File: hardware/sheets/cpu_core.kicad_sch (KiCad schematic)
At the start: 32 parts, among them U1 V20, U10 74HCT32, U11 74HCT125, U12 74HC157, U13 74HCT04, U14 TCM809, U2 74HCT573, U3 74HCT573, U4 74HCT573, U5 74HCT245, U6 74HCT138, U7 74HCT00, U8 74HCT74, U9 74HC161

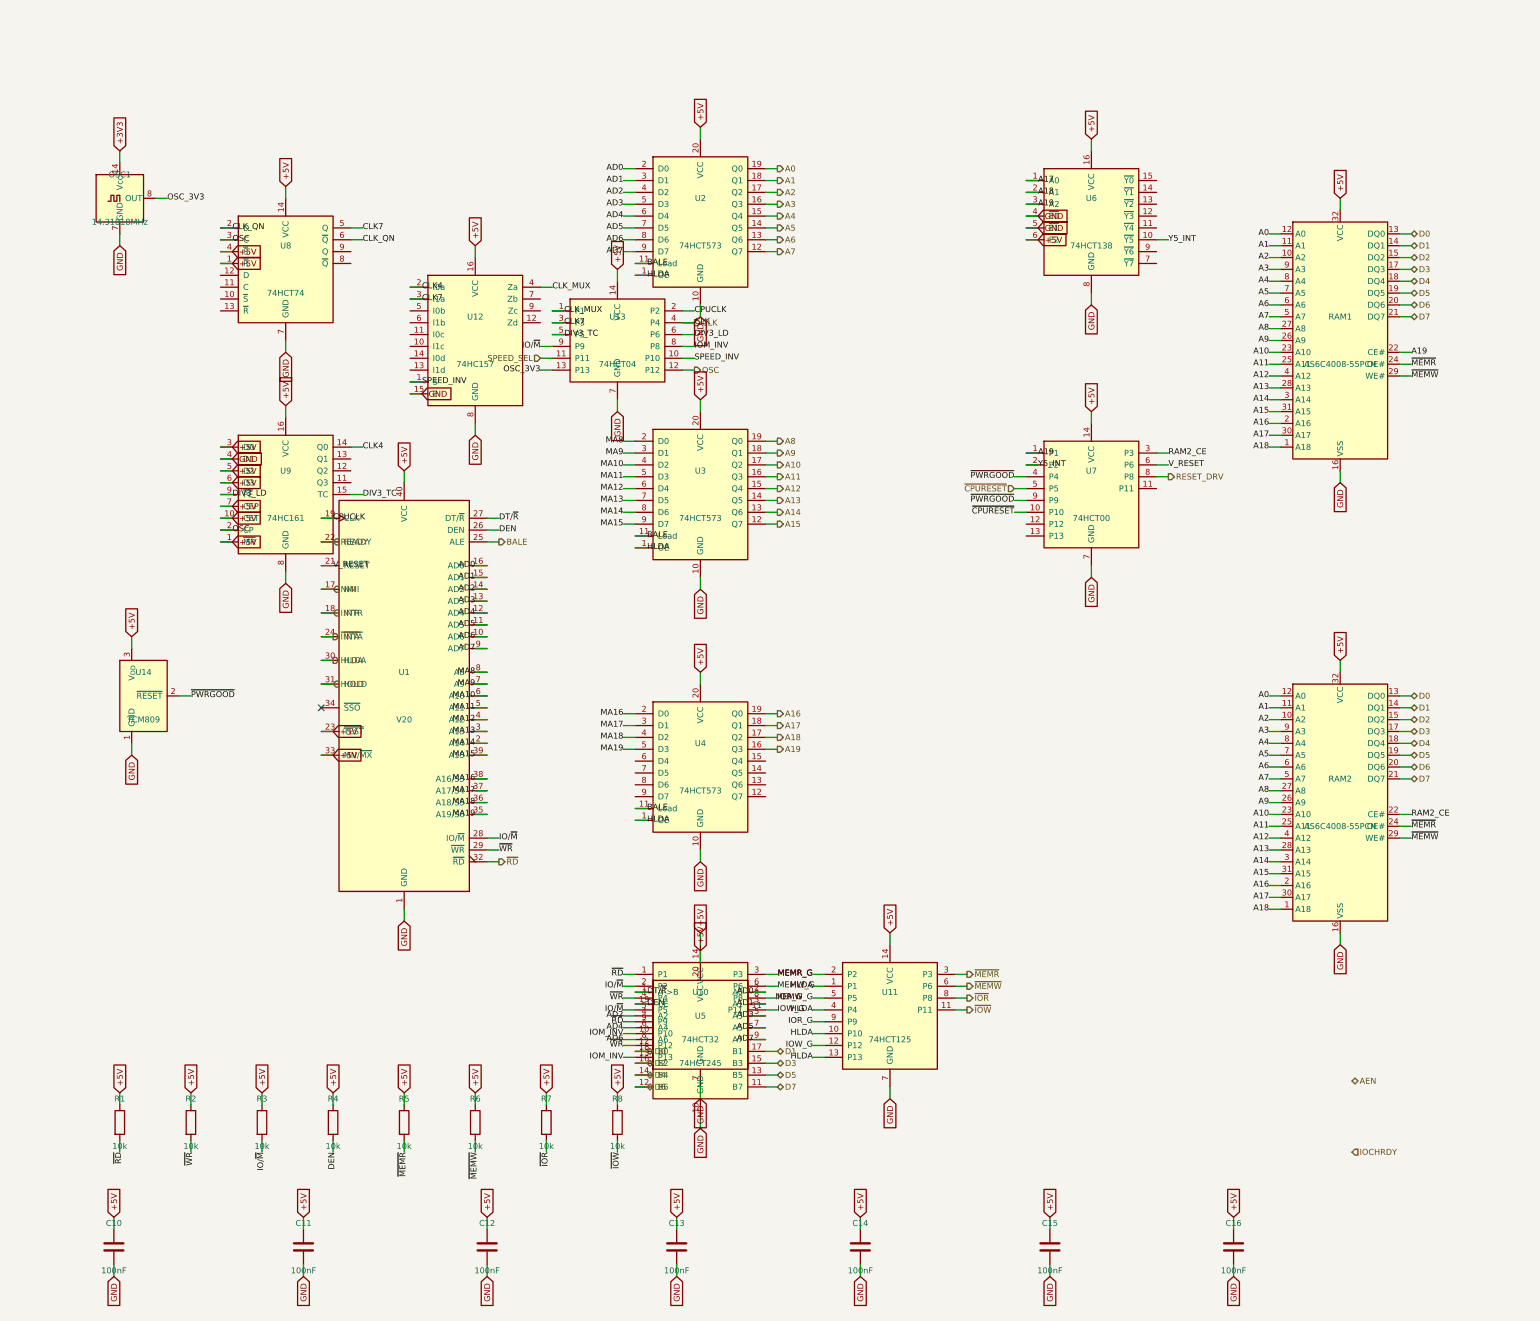
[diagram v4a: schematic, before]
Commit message: Design review 2026-07-11: rail protection, decoupling, wiring fixes
Protection:
- Sidecar +5V now feeds through a 2A polyfuse into +5V_ISA with an
  SMBJ5.0A clamp + 22uF bulk (a faulted ISA card trips its own fuse
  instead of dropping the board; back-fed voltage is clamped).
- USB-C VBUS enters through a 3A polyfuse with an SMBJ5.0A on +5V
  (backstop for the CFG1 9-20V failure mode). CH224K gains a 1uF VDD
  cap; its PG routes to Supervisor GPIO16 as PD_PG. Buck output
  doubled to 2x22uF, 10uF at VIN, extra rail bulk.
- Supervisor USB-A host port: 27R series termination (RP2040
  requirement), USBLC6-2SC6 ESD array, 100uF VBUS bulk.
- Video: HDMI +5V fused (500mA), HPD sensed on GPIO41, 100R series on
  VGA sync. TMDS ESD array deferred to layout (no symbol).
- card_isatest: V5RAW bulk, Q1 gate soft-start cap, TVS on DUT rail.

Wiring fixes:
- SPKR had no driver anywhere (netlist: 1 node). Bus MCU GPIO22
  reassigned from the diagnostics-only bus-CLK sense to SPKR; bus_mcu
  drops CLK from its interface. Doc 5.2 updated.
- bus_mcu C8 decoupled +3V3, a rail that sheet never uses -> 3V3_BUS.
- Storage IRQ5 was push-pull (permanently driven when idle) -> 2N7002
  + gated '125 tri-state, same convention as the LPT IRQ7 stage.
- MAX3241 pump caps resized to the 5V datasheet values (47nF/330nF).
- LPT DB25 status inputs get 4.7k pull-ups (floated with no printer).
- Audio line-out gets a 100R series isolator before the jack.

Best practices:
- Decoupling to ~1x100nF per IC on every sheet + bulk per board
  (cpu_core 7->16 incl. the naked 3.3V oscillator, storage 4->11,
  parallel 6->13, rtc/com/video/bus_mcu/card_isatest similar).
- All floating spare CMOS inputs tied ('00/'74/'157/'02/'04/'125
  sections across cpu_core, bus_mcu, rtc, storage, card_isatest).

Sourcing: new parts mapped in parts.py with JLC-verified LCSC numbers;
Power_Protection lib registered in the tools; TPS563200 stock alert
(4 pcs left at JLC) flagged in parts.py + jlcpcb-sourcing.md. All
decisi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
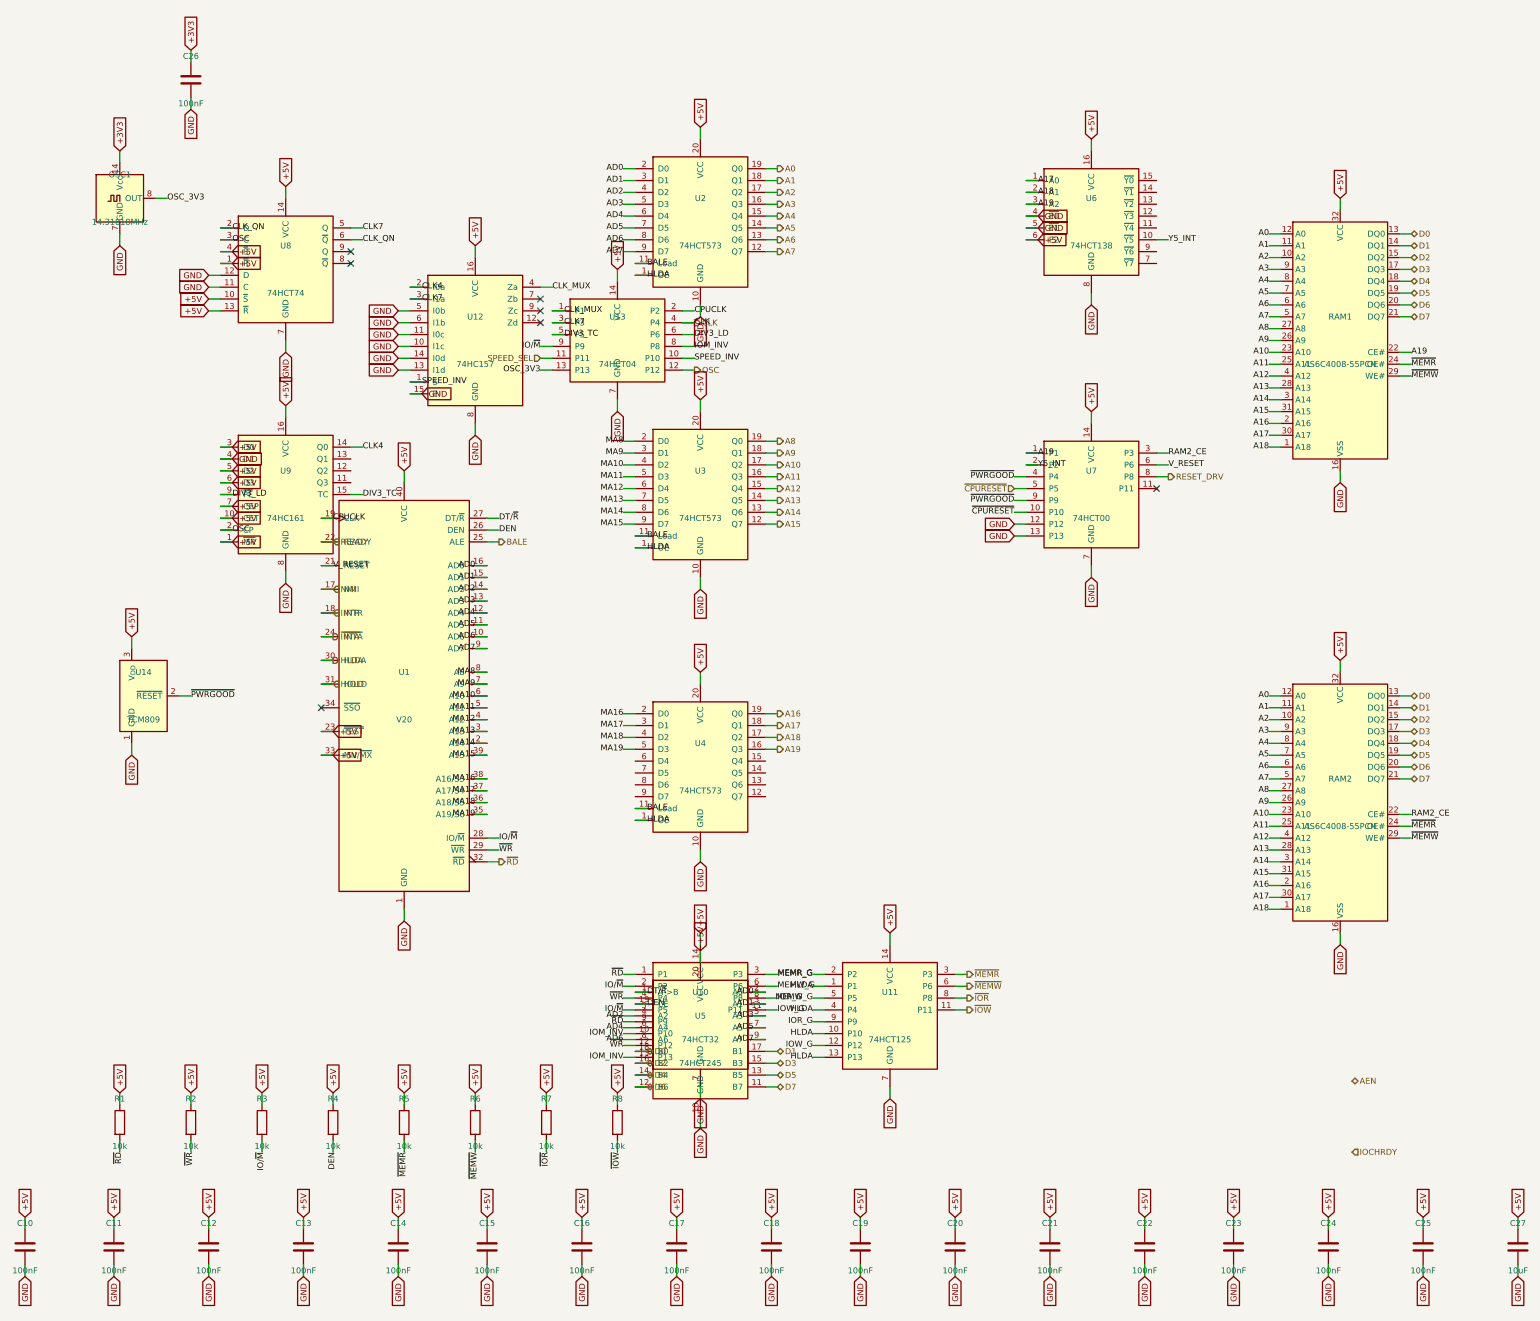
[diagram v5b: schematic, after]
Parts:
- removed R1, R2, R3, R4, R5, R6: 10k, symbol Device:R
- removed U12: 74HC157, symbol mini-xt:74HCT157
- added C11, C12, C13, C14, C15, C16, C17, C18, C19, C20, C21, C22, C23, C24, C25, C26: 100nF, symbol Device:C
- added C27: 10uF, symbol Device:C
- added U13: 74HCT04, symbol mini-xt:74HCT04
- R3: renamed from C10; value 100nF -> 10k; symbol Device:C -> Device:R; LCSC Part Num C14663 -> C25804
- R4: renamed from C11; value 100nF -> 10k; symbol Device:C -> Device:R; LCSC Part Num C14663 -> C25804
- R5: renamed from C12; value 100nF -> 10k; symbol Device:C -> Device:R; LCSC Part Num C14663 -> C25804
- R6: renamed from C13; value 100nF -> 10k; symbol Device:C -> Device:R; LCSC Part Num C14663 -> C25804
- R7: renamed from C14; value 100nF -> 10k; symbol Device:C -> Device:R; LCSC Part Num C14663 -> C25804
- R8: renamed from C15; value 100nF -> 10k; symbol Device:C -> Device:R; LCSC Part Num C14663 -> C25804
- U12: renamed from U13; value 74HCT04 -> 74HC157; symbol mini-xt:74HCT04 -> mini-xt:74HCT157; LCSC Part Num C672096 -> C5609
- renumbered C16 to C10, R7 to R1, R8 to R2
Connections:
- net +3V3: now also C26.1
- net +5V: now also U12.16 (VCC), U8.10 (~{S}), U8.13 (~{R}), C11.1, C12.1, C13.1, C14.1, C15.1, C16.1, C17.1, C18.1, C19.1, C20.1, C21.1, C22.1, C23.1, C24.1, C25.1, C27.1, U13.14 (VCC); no longer U12.14 (VCC)
- net CLK: now also U13.4 (P4); no longer U12.4 (P4)
- net CLK4: now also U12.2 (I0a)
- net CLK7: now also U13.3 (P3)
- net CLK_MUX: now also U12.4 (Za), U13.1 (P1); no longer U12.1 (P1)
- net CPUCLK: now also U13.2 (P2); no longer U12.2 (P2)
- net DEN: now also R4.2
- net DIV3_LD: now also U13.6 (P6); no longer U12.6 (P6)
- net DIV3_TC: now also U13.5 (P5); no longer U12.5 (P5)
- net GND: now also U12.10 (I1c), U12.11 (I0c), U12.13 (I1d), U12.14 (I0d), U12.15 (E), U12.5 (I0b), U12.6 (I1b), U12.8 (GND), U7.12 (P12), U7.13 (P13), U8.11 (C), U8.12 (D), C11.2, C12.2, C13.2, C14.2, C15.2, C16.2, C17.2, C18.2, C19.2, C20.2, C21.2, C22.2, C23.2, C24.2, C25.2, C26.2, C27.2, U13.7 (GND); no longer R3.2, R4.2, R5.2, R6.2, R7.2, R8.2, U12.7 (GND)
- net IO/~{M}: now also R3.2, U13.9 (P9); no longer U12.9 (P9)
- net IOM_INV: now also U13.8 (P8); no longer U12.8 (P8)
- net OSC: now also U13.12 (P12); no longer U12.12 (P12)
- net OSC_3V3: now also U13.13 (P13); no longer U12.13 (P13)
- net SPEED_INV: now also U12.1 (S), U13.10 (P10); no longer U12.10 (P10)
- net SPEED_SEL: now also U13.11 (P11); no longer U12.11 (P11)
- net ~{IOR}: now also R7.2; no longer R1.2
- net ~{IOW}: now also R8.2; no longer R2.2
- net ~{MEMR}: now also R5.2
- net ~{MEMW}: now also R6.2
- net ~{RD}: now also R1.2
- net ~{WR}: now also R2.2
- no-connect marks 1 -> 7
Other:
- moved on the sheet: C10, R1, R2

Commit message: Design-review fixes: reset parking, IRQ8 off the header, analog cleanups
Netlist-wide review sweep. IRQ8 leaves the 60-pin ISA header (pin 15 is a
second GND return; the on-board RTC owns IRQ8 exclusively, so its push-pull
drive is now correct by construction). Bus MCU Hi-Z parking completed:
~CPURESET pulled low (V20 held in reset while the MCU is unprogrammed),
~DACK1/~REFRESH parked deasserted, DRQ1 idled low. Supervisor 12 MHz crystal
damping R actually in series now (was parallel-to-nothing), plus a second
USBLC6 so both prog-port SW2 positions are ESD-protected. Audio: 0.5x PG
summing (MCP6002 headroom), 100k LINE bleed, unit B parked as a follower --
and the SUM stub moved off pin 5's row, where wiring unit B would have
silently merged SUM into VREF. CH224K VDD fed through 1k per the WCH ref
design. VGA blue ladder rescaled 1k/510 -> 820/470 (was ~12% blue-deficient).
Spare CMOS gate inputs grounded uniformly (cpu_core/rtc/storage); UART_RXD
pulled up (SIN idles at mark with JP1 open); dead pins/parts dropped
(com_port CLK, parallel RESET_DRV, storage R3). Bus CLK fixed at 7.16 MHz
logged as a decision. New passives mapped to JLC basic parts in parts.py.

Co-Authored-By: Claude Fable 5 <noreply@anthropic.com>
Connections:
- net GND: now also U4.6 (D4), U4.7 (D5), U4.8 (D6), U4.9 (D7)
- no-connect marks 7 -> 11
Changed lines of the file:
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@@
+	(wire
+		(pts
+			(xy 151.13 166.37)
+			(xy 148.59 166.37)
+		)
+		(stroke
+			(width 0)
+			(type default)
+		)
+	)
+	(global_label "GND"
+		(shape input)
+		(at 148.59 166.37 180)
+		(effects
+			(font
+				(size 1.27 1.27)
+			)
+		)
+	)
+	(no_connect
+		(at 179.07 166.37)
+	)
+	(wire
+		(pts
+			(xy 151.13 168.91)
+			(xy 148.59 168.91)
+		)
+		(stroke
+			(width 0)
+			(type default)
+		)
+	)
+	(global_label "GND"
+		(shape input)
+		(at 148.59 168.91 180)
+		(effects
+			(font
+				(size 1.27 1.27)
+			)
+		)
+	)
+	(no_connect
+		(at 179.07 168.91)
+	)
+	(wire
+		(pts
+			(xy 151.13 171.45)
+			(xy 148.59 171.45)
+		)
+		(stroke
+			(width 0)
+			(type default)
+		)
+	)
+	(global_label "GND"
+		(shape input)
+		(at 148.59 171.45 180)
+		(effects
+			(font
+				(size 1.27 1.27)
+			)
+		)
+	)
+	(no_connect
+		(at 179.07 171.45)
+	)
+	(wire
+		(pts
+			(xy 151.13 173.99)
+			(xy 148.59 173.99)
+		)
+		(stroke
+			(width 0)
+			(type default)
+		)
+	)
+	(global_label "GND"
+		(shape input)
+		(at 148.59 173.99 180)
+		(effects
+			(font
+				(size 1.27 1.27)
+			)
+		)
+	)
+	(no_connect
+		(at 179.07 173.99)
+	)
 	(wire
 		(pts

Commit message: ERC cleanup: NC flags on unused pins, anchored interface labels
KiCad 10 ERC drops from 366 to 16 violations, all noise:

- NC flags on the 36 genuinely unused pins (cpu_core '138/'161 spares,
  Supervisor RP2040 unused GPIO, Core2350B GPIO44-47, rtc '138 spares).
- emit_interface anchors every hier label on a stub wire ending in a
  same-name local label -- connectivity unchanged (still by name;
  netlist spans verified), but nothing dangles.
- Interface honesty: cpu_core drops AEN/IOCHRDY from PINS (both live on
  bus_mcu; nothing here touched them), bus_mcu drops PRIV_COUNTER (the
  counter chain is on-sheet, CNT_* never crosses).
- Remaining 6 label_dangling are root IRQ9-13/15: single-sheet by
  design (soft-PIC pull-ups await future 16-bit sources); kept in PINS
  as the AT-style contract.

Co-Authored-By: Claude Fable 5 <noreply@anthropic.com>
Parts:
- removed OSC1: 14.31818MHz, symbol Oscillator:ACO-xxxMHz
- added U8: 74HCT74, symbol mini-xt:74HCT74
- OSC1: renamed from U8; value 74HCT74 -> 14.31818MHz; symbol mini-xt:74HCT74 -> Oscillator:ACO-xxxMHz; LCSC Part Num C686657 -> C49330311
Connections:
- net +3V3: now also OSC1.14 (Vcc)
- net +5V: now also U8.1 (~{R}), U8.10 (~{S}), U8.13 (~{R}), U8.14 (VCC), U8.4 (~{S}); no longer OSC1.1 (~{R}), OSC1.10 (~{S}), OSC1.13 (~{R}), OSC1.14 (VCC), OSC1.4 (~{S})
- net CLK7: now also U8.5 (Q); no longer OSC1.5 (Q)
- net CLK_QN: now also U8.2 (D), U8.6 (~{Q}); no longer OSC1.2 (D), OSC1.6 (~{Q})
- net GND: now also U8.11 (C), U8.12 (D), U8.7 (GND); no longer OSC1.11 (C), OSC1.12 (D)
- net OSC: now also U8.3 (C); no longer OSC1.3 (C)
- net OSC_3V3: now also OSC1.8 (OUT)
- no-connect marks 11 -> 21
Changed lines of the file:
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@@
 		)
+	)
+	(no_connect
+		(at 262.89 41.91)
+	)
+	(no_connect
+		(at 262.89 44.45)
+	)
+	(no_connect
+		(at 262.89 46.99)
+	)
+	(no_connect
+		(at 262.89 49.53)
+	)
+	(no_connect
+		(at 262.89 52.07)
+	)
+	(no_connect
+		(at 262.89 57.15)
+	)
+	(no_connect
+		(at 262.89 59.69)
 	)
 	(wire
@@
 		)
 	)
+	(no_connect
+		(at 90.17 101.6)
+	)
+	(no_connect
+		(at 90.17 104.14)
+	)
+	(no_connect
+		(at 90.17 106.68)
+	)
 	(wire
 		(pts
@@
 		(effects
 			(font
-				(size 1.27 1.27)
-			)
-		)
-	)
-	(hierarchical_label "IOCHRDY"
-		(shape input)
-		(at 304.8 250.19 0)
-		(effects
-			(font
-				(size 1.27 1.27)
-			)
-		)
-	)
-	(hierarchical_label "AEN"
-		(shape bidirectional)
-		(at 304.8 234.95 0)
-		(effects
-			(font
